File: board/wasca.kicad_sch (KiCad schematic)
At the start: 66 parts, among them CN1 CARTRIDGE_EDGE_CONNECTOR, CN2 TFP09-2-12B, CN3 Conn_02x02_Odd_Even, CN4 SODIMM-200, CN5 693063020911, CN6 Conn_01x02_Pin, U1 74ALVC164245, U10 SN74LVC1T45DBV, U11 SN74LVC1T45DBV, U12 SN74LVC1T45DBV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

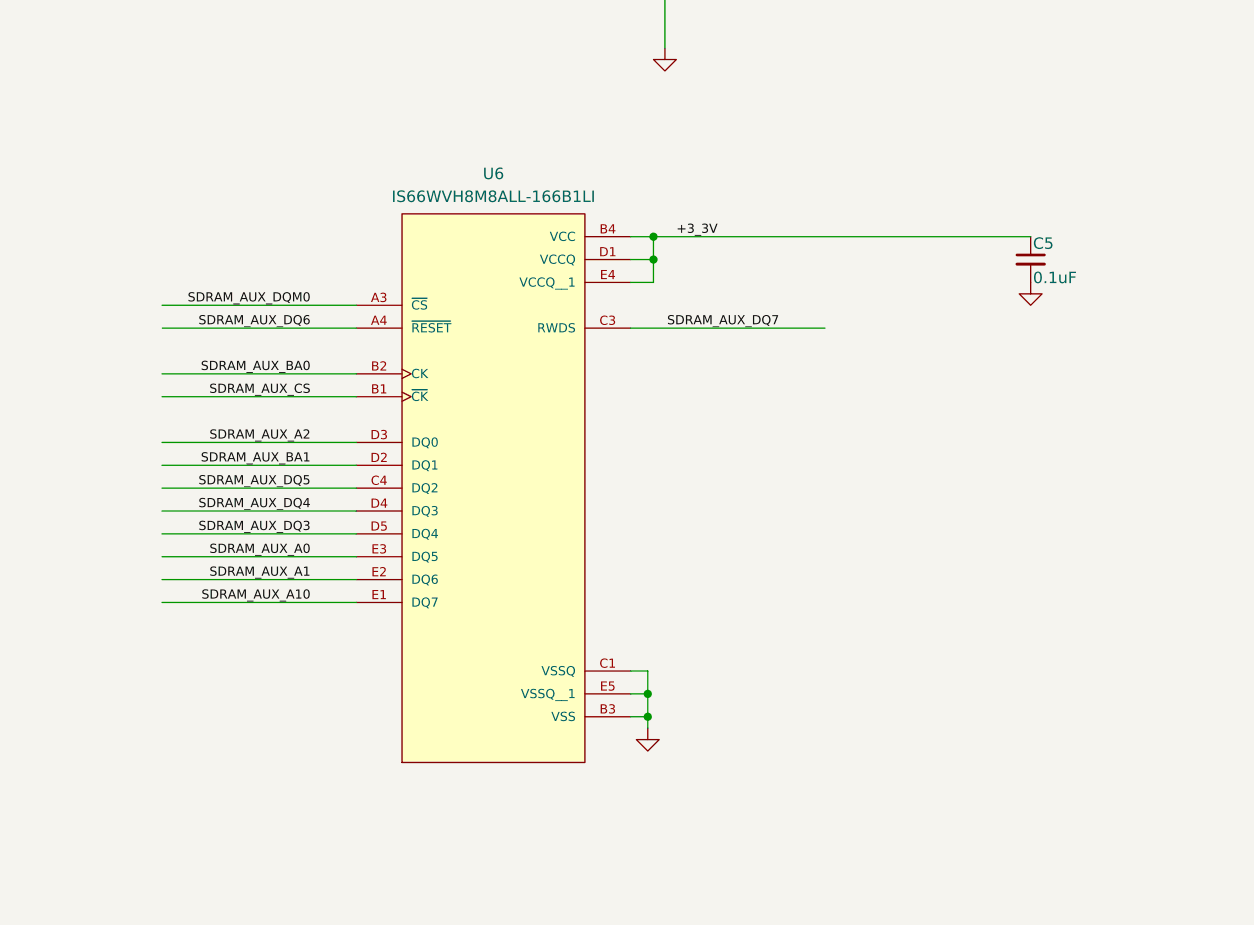
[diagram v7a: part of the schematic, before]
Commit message: Remove HyperRAM
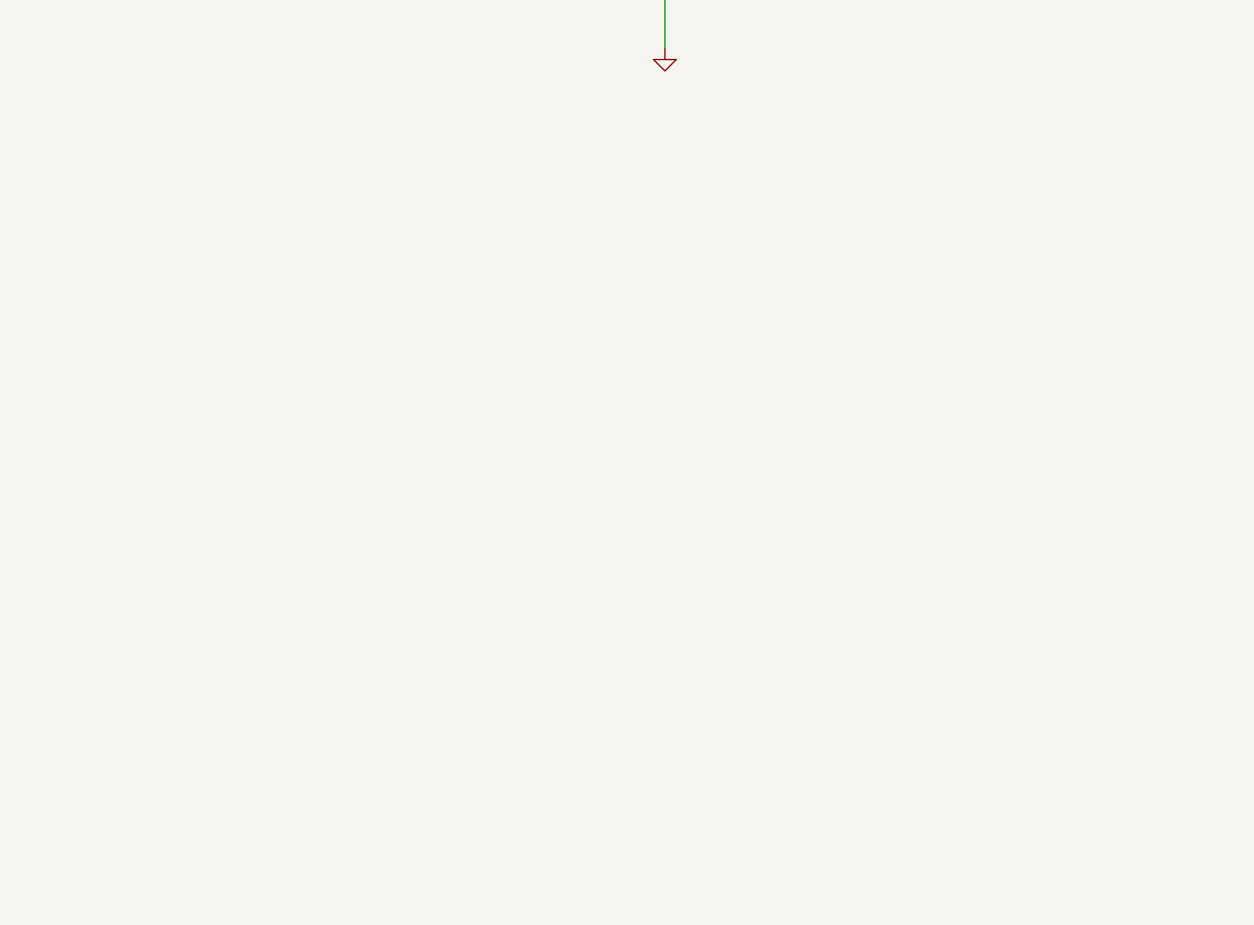
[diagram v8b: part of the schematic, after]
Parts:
- removed C5: 0.1uF, Capacitor_SMD:C_0603_1608Metric_Pad1.08x0.95mm_HandSolder, symbol Device:C_Small
- removed U6: IS66WVH8M8ALL-166B1LI, wasca:BGA25C100P5X5_800X600X120N, symbol IS66WVH8M8ALL-166B1LI:IS66WVH8M8ALL-166B1LI
- CN2: footprint TFP09212B -> wasca:TFP09212B
